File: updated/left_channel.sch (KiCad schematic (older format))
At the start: 20 parts, among them J2 Left 8 ohms, J3 Left 0 ohms, J7 Conn_Coaxial, T1 AudioTxfmr

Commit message: finish updated schematic
Convert tables from google doc to markdown to have these in this repo
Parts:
- removed RV1A: R_POT, symbol Device:R_POT
- removed V1: 6H8C, symbol local:6H8C
- removed V2,V3: 6P1, symbol local:6P1
- added RV1: R_POT_Dual_Separate, symbol Device:R_POT_Dual_Separate
- added V1: 12AX7, Valve:Valve_ECC-83-1, symbol local:12AX7
- added V2: EL84, Valve:Valve_ECC-83-1, symbol local:EL84
- C1: footprint (none) -> Capacitor_THT:CP_Radial_D8.0mm_P5.00mm
- C2: footprint (none) -> Capacitor_THT:CP_Radial_D4.0mm_P2.00mm
- C3: footprint (none) -> Capacitor_THT:CP_Radial_D10.0mm_P2.50mm
- C4: footprint (none) -> Capacitor_THT:CP_Radial_D10.0mm_P5.00mm
- C5: renamed from C8; footprint (none) -> Capacitor_THT:CP_Radial_D10.0mm_P5.00mm
- R1, R13, R2, R3, R5, R6: footprint (none) -> Resistor_THT:R_Axial_DIN0516_L15.5mm_D5.0mm_P20.32mm_Horizontal
- R14: renamed from R14,R15; footprint (none) -> Resistor_THT:R_Axial_DIN0516_L15.5mm_D5.0mm_P20.32mm_Horizontal
- R4: renamed from R9; footprint (none) -> Resistor_THT:R_Axial_DIN0516_L15.5mm_D5.0mm_P20.32mm_Horizontal
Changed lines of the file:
@@
 P 4300 2000
 AR Path="/5F1FED3C" Ref="C?"  Part="1"
-AR Path="/5F1F04D2/5F1FED3C" Ref="C8"  Part="1"
-F 0 "C8" H 4418 2091 50  0000 L CNN
+AR Path="/5F1F04D2/5F1FED3C" Ref="C5"  Part="1"
+F 0 "C5" H 4418 2091 50  0000 L CNN
 F 1 "22uF" H 4418 2000 50  0000 L CNN
-F 2 "" H 4338 1850 50  0001 C CNN
+F 2 "Capacitor_THT:CP_Radial_D10.0mm_P5.00mm" H 4338 1850 50  0001 C CNN
 F 3 "~" H 4300 2000 50  0001 C CNN
 F 4 "450V" H 4418 1909 50  0000 L CNN "Voltage"
@@
 F 0 "R6" V 3743 1850 50  0000 C CNN
 F 1 "1.5K" V 3834 1850 50  0000 C CNN
-F 2 "" V 3880 1850 50  0001 C CNN
+F 2 "Resistor_THT:R_Axial_DIN0516_L15.5mm_D5.0mm_P20.32mm_Horizontal" V 3880 1850 50  0001 C CNN
 F 3 "~" H 3950 1850 50  0001 C CNN
 	1    3950 1850
@@
 P 4300 2150
 AR Path="/5F1FED49" Ref="#PWR?"  Part="1"
-AR Path="/5F1F04D2/5F1FED49" Ref="#PWR?"  Part="1"
-F 0 "#PWR?" H 4300 1900 50  0001 C CNN
+AR Path="/5F1F04D2/5F1FED49" Ref="#PWR07"  Part="1"
+F 0 "#PWR07" H 4300 1900 50  0001 C CNN
 F 1 "Earth" H 4300 2000 50  0001 C CNN
 F 2 "" H 4300 2150 50  0001 C CNN
@@
 P 4800 2000
 AR Path="/5F1FED4F" Ref="R?"  Part="1"
-AR Path="/5F1F04D2/5F1FED4F" Ref="R9"  Part="1"
-F 0 "R9" H 4730 1954 50  0000 R CNN
+AR Path="/5F1F04D2/5F1FED4F" Ref="R4"  Part="1"
+F 0 "R4" H 4730 1954 50  0000 R CNN
 F 1 "30K" H 4730 2045 50  0000 R CNN
-F 2 "" V 4730 2000 50  0001 C CNN
+F 2 "Resistor_THT:R_Axial_DIN0516_L15.5mm_D5.0mm_P20.32mm_Horizontal" V 4730 2000 50  0001 C CNN
 F 3 "~" H 4800 2000 50  0001 C CNN
 	1    4800 2000
@@
 $EndComp
 Connection ~ 4300 1850
-$Comp
-L local:6H8C V?
-U 1 1 5F1FED56
-P 4800 3100
-AR Path="/5F1FED56" Ref="V?"  Part="1"
-AR Path="/5F1F04D2/5F1FED56" Ref="V1"  Part="1"
-F 0 "V1" H 5108 3096 50  0000 L CNN
-F 1 "6H8C" H 5108 3005 50  0000 L CNN
-F 2 "" H 4820 3100 50  0001 C CNN
-F 3 "" H 4820 3100 50  0001 C CNN
-	1    4800 3100
-	1    0    0    -1
-$EndComp
 $Comp
 L Device:C C?
@@
 F 0 "C2" V 4898 2350 50  0000 C CNN
 F 1 "0.1uF" V 5000 2300 50  0000 C CNN
-F 2 "" H 5188 2200 50  0001 C CNN
+F 2 "Capacitor_THT:CP_Radial_D4.0mm_P2.00mm" H 5188 2200 50  0001 C CNN
 F 3 "~" H 5150 2350 50  0001 C CNN
 F 4 "450V" V 5000 2600 50  0000 C CNN "Voltage"
@@
 F 0 "R2" V 4343 2550 50  0000 C CNN
 F 1 "470K" V 4434 2550 50  0000 C CNN
-F 2 "" V 4480 2550 50  0001 C CNN
+F 2 "Resistor_THT:R_Axial_DIN0516_L15.5mm_D5.0mm_P20.32mm_Horizontal" V 4480 2550 50  0001 C CNN
 F 3 "~" H 4550 2550 50  0001 C CNN
 	1    4550 2550
@@
 F 0 "C3" H 3850 2950 50  0000 L CNN
 F 1 "220K400" H 3850 2850 50  0000 L CNN
-F 2 "" H 4338 2750 50  0001 C CNN
+F 2 "Capacitor_THT:CP_Radial_D10.0mm_P2.50mm" H 4338 2750 50  0001 C CNN
 F 3 "~" H 4300 2900 50  0001 C CNN
 	1    4300 2900
@@
 F 0 "R13" H 4370 3446 50  0000 L CNN
 F 1 "1M" H 4370 3355 50  0000 L CNN
-F 2 "" V 4230 3400 50  0001 C CNN
+F 2 "Resistor_THT:R_Axial_DIN0516_L15.5mm_D5.0mm_P20.32mm_Horizontal" V 4230 3400 50  0001 C CNN
 F 3 "~" H 4300 3400 50  0001 C CNN
 	1    4300 3400
 	1    0    0    -1
 $EndComp
-$Comp
-L local:6H8C V?
-U 2 1 5F1FED76
-P 4800 4450
-AR Path="/5F1FED76" Ref="V?"  Part="2"
-AR Path="/5F1F04D2/5F1FED76" Ref="V1"  Part="2"
-F 0 "V1" H 5108 4446 50  0000 L CNN
-F 1 "6H8C" H 5108 4355 50  0000 L CNN
-F 2 "" H 4820 4450 50  0001 C CNN
-F 3 "" H 4820 4450 50  0001 C CNN
-	2    4800 4450
-	1    0    0    -1
-$EndComp
 Wire Wire Line
 	4300 3550 4300 4000
 Wire Wire Line
 	5050 3650 5050 4000
-Wire Wire Line
-	4800 4000 5050 4000
 $Comp
 L Connector:Conn_Coaxial J?
@@
 	-1   0    0    -1
 $EndComp
-$Comp
-L Device:R_POT RV1A?
-U 1 1 5F1FED85
-P 4000 4500
-AR Path="/5F1FED85" Ref="RV1A?"  Part="1"
-AR Path="/5F1F04D2/5F1FED85" Ref="RV1A"  Part="1"
-F 0 "RV1A" H 3931 4546 50  0000 R CNN
-F 1 "R_POT" H 3931 4455 50  0000 R CNN
-F 2 "" H 4000 4500 50  0001 C CNN
-F 3 "~" H 4000 4500 50  0001 C CNN
-	1    4000 4500
-	1    0    0    -1
-$EndComp
 Wire Wire Line
 	4000 4650 4000 5900
@@
 P 3450 5900
 AR Path="/5F1FED8E" Ref="#PWR?"  Part="1"
-AR Path="/5F1F04D2/5F1FED8E" Ref="#PWR?"  Part="1"
-F 0 "#PWR?" H 3450 5650 50  0001 C CNN
+AR Path="/5F1F04D2/5F1FED8E" Ref="#PWR06"  Part="1"
+F 0 "#PWR06" H 3450 5650 50  0001 C CNN
 F 1 "Earth" H 3450 5750 50  0001 C CNN
 F 2 "" H 3450 5900 50  0001 C CNN
@@
 Wire Wire Line
 	4150 4500 4300 4500
-Text Label 4700 3700 2    50   ~ 0
+Text Label 4700 3650 2    50   ~ 0
 fl1
-Text Label 4900 3700 2    50   ~ 0
+Text Label 4900 3650 2    50   ~ 0
 fl2
 Text Label 4700 5000 2    50   ~ 0
@@
 F 0 "R5" H 4370 4896 50  0000 L CNN
 F 1 "470K" H 4370 4805 50  0000 L CNN
-F 2 "" V 4230 4850 50  0001 C CNN
+F 2 "Resistor_THT:R_Axial_DIN0516_L15.5mm_D5.0mm_P20.32mm_Horizontal" V 4230 4850 50  0001 C CNN
 F 3 "~" H 4300 4850 50  0001 C CNN
 	1    4300 4850
@@
 F 0 "R3" H 4920 5546 50  0000 L CNN
 F 1 "2.2K" H 4920 5455 50  0000 L CNN
-F 2 "" V 4780 5500 50  0001 C CNN
+F 2 "Resistor_THT:R_Axial_DIN0516_L15.5mm_D5.0mm_P20.32mm_Horizontal" V 4780 5500 50  0001 C CNN
 F 3 "~" H 4850 5500 50  0001 C CNN
 	1    4850 5500
@@
 F 0 "C4" H 5318 5591 50  0000 L CNN
 F 1 "100uF" H 5318 5500 50  0000 L CNN
-F 2 "" H 5238 5350 50  0001 C CNN
+F 2 "Capacitor_THT:CP_Radial_D10.0mm_P5.00mm" H 5238 5350 50  0001 C CNN
 F 3 "~" H 5200 5500 50  0001 C CNN
 F 4 "25V" H 5318 5409 50  0000 L CNN "Voltage"
@@
 Wire Wire Line
 	4300 3050 4300 3150
-Wire Wire Line
-	4800 4000 4300 4000
-Connection ~ 4800 4000
 Wire Wire Line
 	4450 3150 4300 3150
@@
 Wire Wire Line
 	7750 2000 7650 2000
-$Comp
-L local:6P1 V2,V?
-U 1 1 5F1FEDE2
-P 7050 3100
-AR Path="/5F1FEDE2" Ref="V2,V?"  Part="1"
-AR Path="/5F1F04D2/5F1FEDE2" Ref="V2,V3"  Part="1"
-F 0 "V2,V3" H 7358 3096 50  0000 L CNN
-F 1 "6P1" H 7358 3005 50  0000 L CNN
-F 2 "" H 7070 3000 50  0001 C CNN
-F 3 "" H 7070 3000 50  0001 C CNN
-	1    7050 3100
-	1    0    0    -1
-$EndComp
 Wire Wire Line
 	6700 3300 5800 3300
@@
 P 6600 2950
 AR Path="/5F1FEDEC" Ref="R?"  Part="1"
-AR Path="/5F1F04D2/5F1FEDEC" Ref="R14,R15"  Part="1"
-F 0 "R14,R15" H 6670 2996 50  0000 L CNN
+AR Path="/5F1F04D2/5F1FEDEC" Ref="R14"  Part="1"
+F 0 "R14" H 6670 2996 50  0000 L CNN
 F 1 "100" H 6670 2905 50  0000 L CNN
-F 2 "" V 6530 2950 50  0001 C CNN
+F 2 "Resistor_THT:R_Axial_DIN0516_L15.5mm_D5.0mm_P20.32mm_Horizontal" V 6530 2950 50  0001 C CNN
 F 3 "~" H 6600 2950 50  0001 C CNN
 	1    6600 2950
@@
 Wire Wire Line
 	7050 2300 7050 2650
-Connection ~ 7050 2650
 $Comp
 L Device:CP C?
@@
 F 0 "C1" H 7568 4191 50  0000 L CNN
 F 1 "220uF" H 7568 4100 50  0000 L CNN
-F 2 "" H 7488 3950 50  0001 C CNN
+F 2 "Capacitor_THT:CP_Radial_D8.0mm_P5.00mm" H 7488 3950 50  0001 C CNN
 F 3 "~" H 7450 4100 50  0001 C CNN
 F 4 "50V" H 7568 4009 50  0000 L CNN "Voltage"
@@
 F 0 "R1" H 7170 4146 50  0000 L CNN
 F 1 "270" H 7170 4055 50  0000 L CNN
-F 2 "" V 7030 4100 50  0001 C CNN
+F 2 "Resistor_THT:R_Axial_DIN0516_L15.5mm_D5.0mm_P20.32mm_Horizontal" V 7030 4100 50  0001 C CNN
 F 3 "~" H 7100 4100 50  0001 C CNN
 F 4 "5W" H 7100 4100 50  0001 C CNN "Power"
@@
 Wire Wire Line
 	3650 1850 3550 1850
+$Comp
+L local:EL84 V2
+U 1 1 5F1E5866
+P 7050 3100
+F 0 "V2" H 7358 3096 50  0000 L CNN
+F 1 "EL84" H 7358 3005 50  0000 L CNN
+F 2 "Valve:Valve_ECC-83-1" H 7070 3000 50  0001 C CNN
+F 3 "" H 7070 3000 50  0001 C CNN
+	1    7050 3100
+	1    0    0    -1
+$EndComp
+Connection ~ 7050 2650
+$Comp
+L local:12AX7 V1
+U 1 1 5F1EB7D2
+P 4800 3100
+F 0 "V1" H 5108 3096 50  0000 L CNN
+F 1 "12AX7" H 5108 3005 50  0000 L CNN
+F 2 "Valve:Valve_ECC-83-1" H 4820 3100 50  0001 C CNN
+F 3 "" H 4820 3100 50  0001 C CNN
+	1    4800 3100
+	1    0    0    -1
+$EndComp
+Wire Wire Line
+	4300 4000 4800 4000
+$Comp
+L local:12AX7 V1
+U 2 1 5F1F6427
+P 4800 4450
+F 0 "V1" H 5108 4446 50  0000 L CNN
+F 1 "12AX7" H 5108 4355 50  0000 L CNN
+F 2 "Valve:Valve_ECC-83-1" H 4820 4450 50  0001 C CNN
+F 3 "" H 4820 4450 50  0001 C CNN
+	2    4800 4450
+	1    0    0    -1
+$EndComp
+Connection ~ 4800 4000
+Wire Wire Line
+	4800 4000 5050 4000
+$Comp
+L Device:R_POT_Dual_Separate RV1
+U 1 1 5F23DDB3
+P 4000 4500
+F 0 "RV1" H 3930 4546 50  0000 R CNN
+F 1 "R_POT_Dual_Separate" H 3930 4455 50  0000 R CNN
+F 2 "" H 4000 4500 50  0001 C CNN
+F 3 "~" H 4000 4500 50  0001 C CNN
+	1    4000 4500
+	1    0    0    -1
+$EndComp
 $EndSCHEMATC

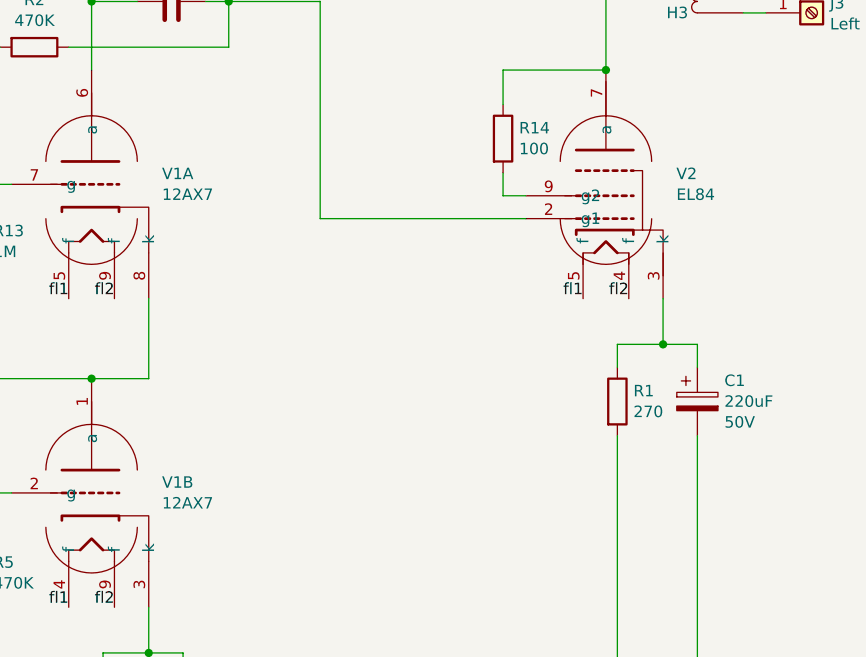
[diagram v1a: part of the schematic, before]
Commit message: add schematic for updated amp
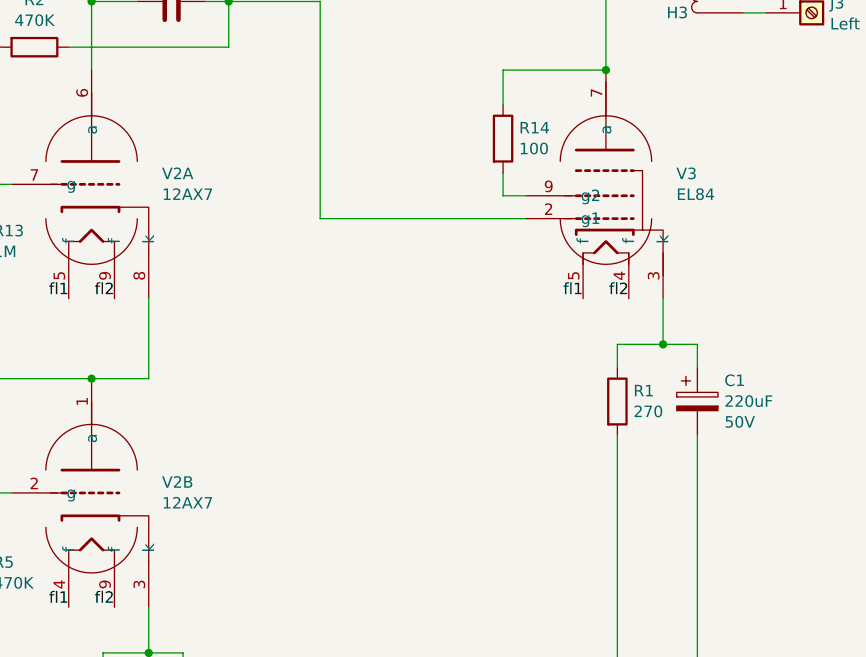
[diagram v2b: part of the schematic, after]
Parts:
- renumbered V1 to V2, V2 to V3
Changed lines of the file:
@@
 	3650 1850 3550 1850
 $Comp
-L local:EL84 V2
+L local:EL84 V3
 U 1 1 5F1E5866
 P 7050 3100
-F 0 "V2" H 7358 3096 50  0000 L CNN
+F 0 "V3" H 7358 3096 50  0000 L CNN
 F 1 "EL84" H 7358 3005 50  0000 L CNN
 F 2 "Valve:Valve_ECC-83-1" H 7070 3000 50  0001 C CNN
@@
 Connection ~ 7050 2650
 $Comp
-L local:12AX7 V1
+L local:12AX7 V2
 U 1 1 5F1EB7D2
 P 4800 3100
-F 0 "V1" H 5108 3096 50  0000 L CNN
+F 0 "V2" H 5108 3096 50  0000 L CNN
 F 1 "12AX7" H 5108 3005 50  0000 L CNN
 F 2 "Valve:Valve_ECC-83-1" H 4820 3100 50  0001 C CNN
@@
 	4300 4000 4800 4000
 $Comp
-L local:12AX7 V1
+L local:12AX7 V2
 U 2 1 5F1F6427
 P 4800 4450
-F 0 "V1" H 5108 4446 50  0000 L CNN
+F 0 "V2" H 5108 4446 50  0000 L CNN
 F 1 "12AX7" H 5108 4355 50  0000 L CNN
 F 2 "Valve:Valve_ECC-83-1" H 4820 4450 50  0001 C CNN

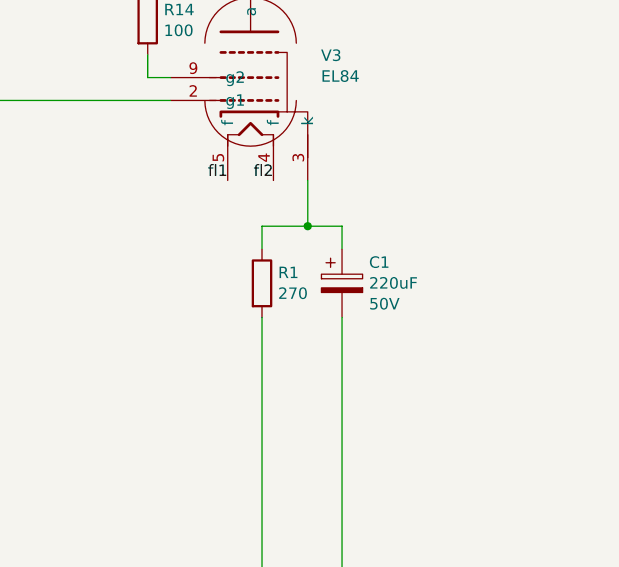
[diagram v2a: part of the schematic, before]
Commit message: install new electrolytic capacitors
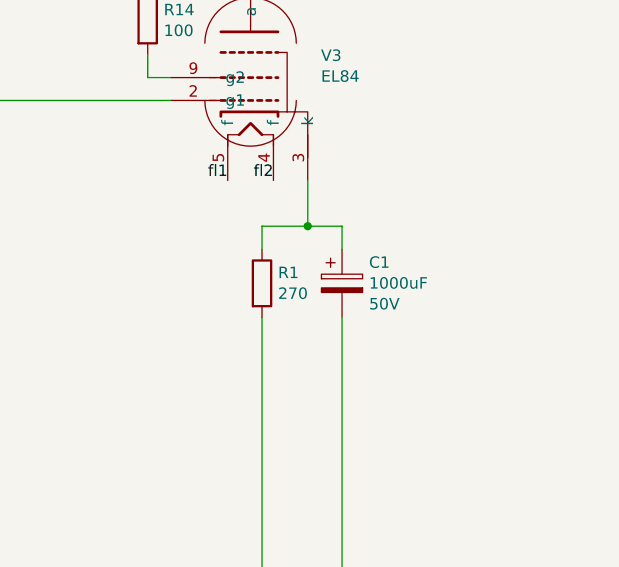
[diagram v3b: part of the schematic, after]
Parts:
- C1: value 220uF -> 1000uF
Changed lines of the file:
@@
 AR Path="/5F1F04D2/5F1FEDF9" Ref="C1"  Part="1"
 F 0 "C1" H 7568 4191 50  0000 L CNN
-F 1 "220uF" H 7568 4100 50  0000 L CNN
+F 1 "1000uF" H 7568 4100 50  0000 L CNN
 F 2 "Capacitor_THT:CP_Radial_D8.0mm_P5.00mm" H 7488 3950 50  0001 C CNN
 F 3 "~" H 7450 4100 50  0001 C CNN
